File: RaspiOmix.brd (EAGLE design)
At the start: 85 x 56 mm, 48 parts, among them IC1 MCP3424-E/SL, IC2 DS1307

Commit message: Small modif !
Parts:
- moved R27 5.07 mm to (67.5, 20.3), turned to 180 degrees
- moved R26 1.02 mm to (67.5, 18.1)
- moved C5 0.95 mm to (64.1, 19.7)
- moved C30 0.32 mm to (53.3, 35.6)
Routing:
- net PI_SCL: track 87.6 -> 88.6 mm
- net +5V: track 283.7 -> 282.9 mm
- net N$4: track 10.5 -> 9.76 mm

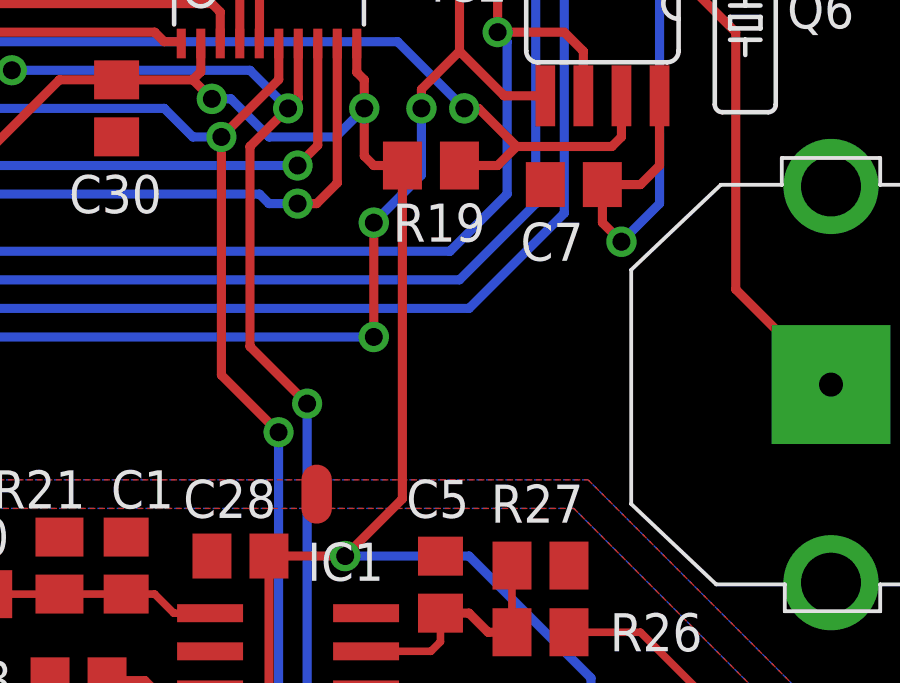
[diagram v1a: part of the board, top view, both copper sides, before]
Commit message: Added C6
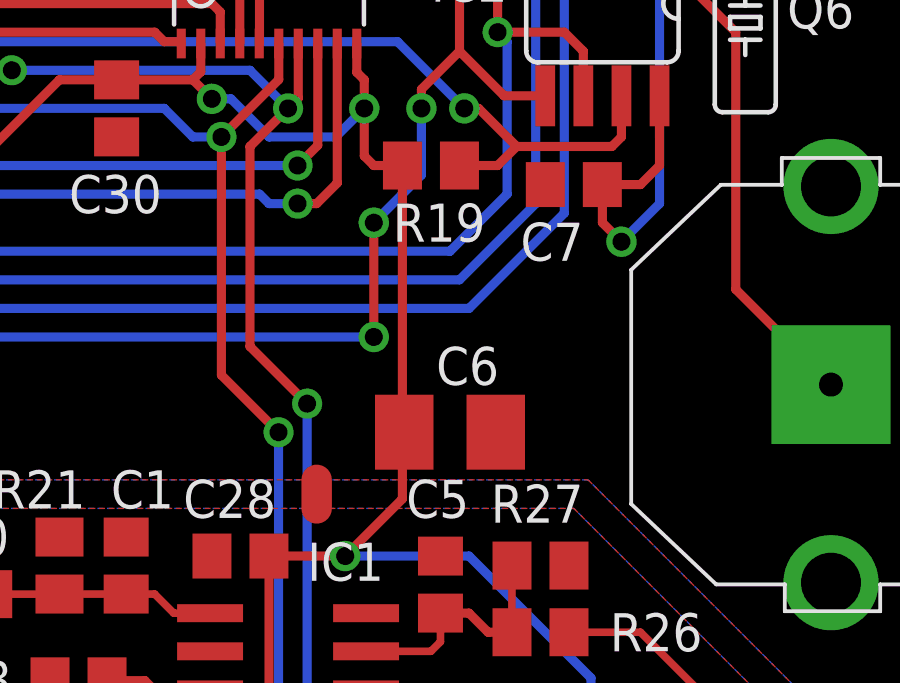
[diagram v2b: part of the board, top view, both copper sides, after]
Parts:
- added C6: (no value), rcl:B/3528-21R
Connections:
- net +3V3: now also C6.+
- net VSS: now also C6.-
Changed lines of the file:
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@@
 <layer number="22" name="bPlace" color="7" fill="1" visible="yes" active="yes"/>
 <layer number="23" name="tOrigins" color="15" fill="1" visible="yes" active="yes"/>
-<layer number="24" name="bOrigins" color="15" fill="1" visible="yes" active="yes"/>
+<layer number="24" name="bOrigins" color="15" fill="1" visible="no" active="yes"/>
 <layer number="25" name="tNames" color="7" fill="1" visible="yes" active="yes"/>
 <layer number="26" name="bNames" color="7" fill="1" visible="yes" active="yes"/>
@@
 <layer number="37" name="tTest" color="7" fill="1" visible="no" active="yes"/>
 <layer number="38" name="bTest" color="7" fill="1" visible="no" active="yes"/>
-<layer number="39" name="tKeepout" color="4" fill="11" visible="yes" active="yes"/>
-<layer number="40" name="bKeepout" color="1" fill="11" visible="no" active="yes"/>
-<layer number="41" name="tRestrict" color="4" fill="10" visible="yes" active="yes"/>
-<layer number="42" name="bRestrict" color="1" fill="10" visible="no" active="yes"/>
+<layer number="39" name="tKeepout" color="4" fill="11" visible="no" active="yes"/>
+<layer number="40" name="bKeepout" color="1" fill="11" visible="yes" active="yes"/>
+<layer number="41" name="tRestrict" color="4" fill="10" visible="no" active="yes"/>
+<layer number="42" name="bRestrict" color="1" fill="10" visible="yes" active="yes"/>
 <layer number="43" name="vRestrict" color="2" fill="10" visible="yes" active="yes"/>
 <layer number="44" name="Drills" color="7" fill="1" visible="no" active="yes"/>
@@
 <attribute name="VALUE" x="67.5274" y="10.795" size="0.02" layer="28" rot="MR180"/>
 </element>
+<element name="C6" library="rcl" package="B/3528-21R" value="" x="64.4525" y="24.765" smashed="yes" rot="R180">
+<attribute name="NAME" x="66.085" y="27.61" size="1.27" layer="25" rot="R180"/>
+<attribute name="VALUE" x="66.4025" y="27.69" size="1.27" layer="27" rot="R180"/>
+</element>
 </elements>
 <signals>
@@
 <contactref element="J_ADR0" pad="1"/>
 <contactref element="J_ADR1" pad="1"/>
+<contactref element="C6" pad="-"/>
 <wire x1="8.89" y1="54.61" x2="9.8425" y2="54.9275" width="0" layer="19" extent="1-1"/>
 <wire x1="3.81" y1="49.8475" x2="3.81" y2="48.895" width="0" layer="19" extent="1-16"/>
@@
 <wire x1="62.8675" y1="33.655" x2="62.8675" y2="33.0225" width="0.3048" layer="1"/>
 <wire x1="62.8675" y1="33.0225" x2="62.865" y2="33.02" width="0.3048" layer="1"/>
-<wire x1="62.865" y1="33.02" x2="62.865" y2="22.5425" width="0.3048" layer="1"/>
+<wire x1="62.865" y1="33.02" x2="62.865" y2="24.765" width="0.3048" layer="1"/>
+<wire x1="62.865" y1="24.765" x2="62.865" y2="22.5425" width="0.3048" layer="1"/>
 <wire x1="2.2225" y1="34.925" x2="2.2225" y2="38.4175" width="0.3048" layer="16"/>
 <wire x1="2.2225" y1="38.4175" x2="3.175" y2="39.37" width="0.3048" layer="16"/>
@@
 <wire x1="65.0875" y1="20.6375" x2="60.96" y2="20.6375" width="0.3048" layer="16"/>
 <via x="60.96" y="20.6375" extent="1-16" drill="0.6" diameter="1.016"/>
+<contactref element="C6" pad="+"/>
+<wire x1="62.9275" y1="24.765" x2="62.865" y2="24.765" width="0.254" layer="1"/>
 </signal>
 <signal name="PI_TX">

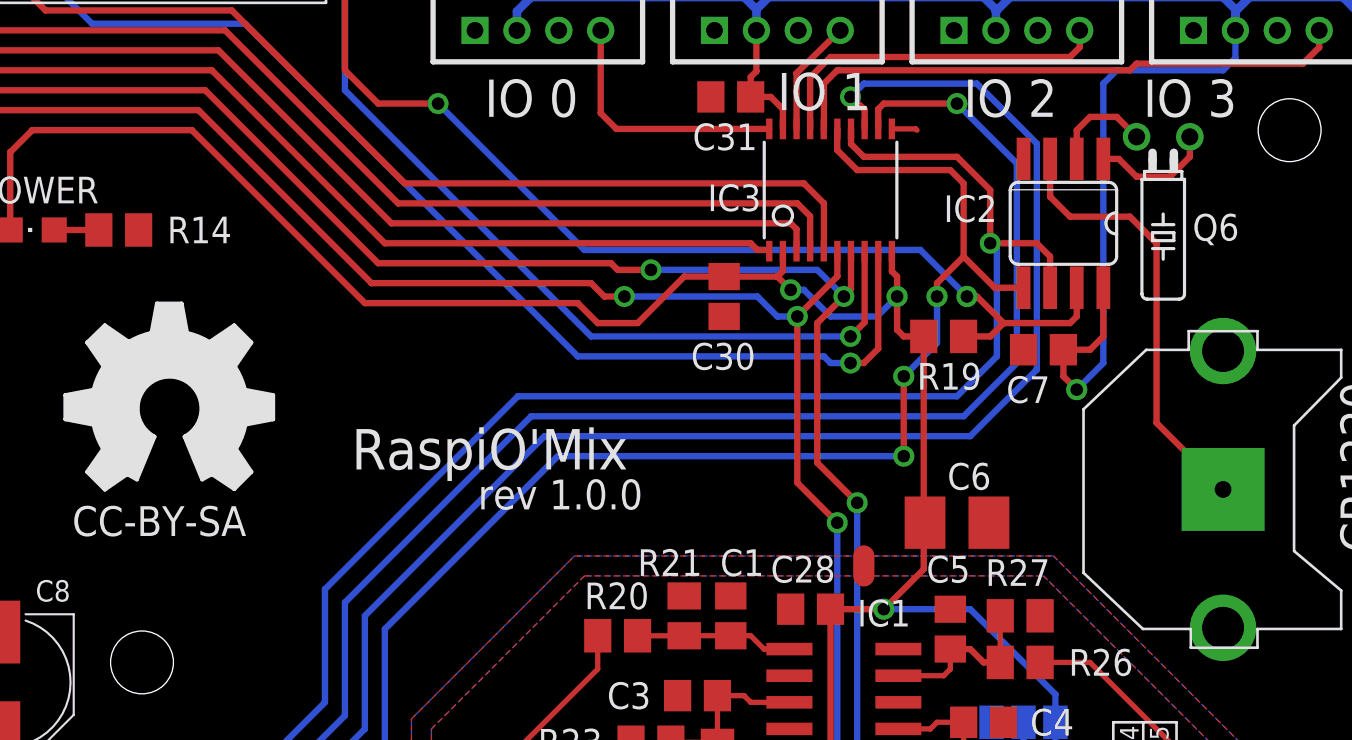
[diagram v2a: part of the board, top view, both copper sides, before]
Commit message: Version avec Mosfet
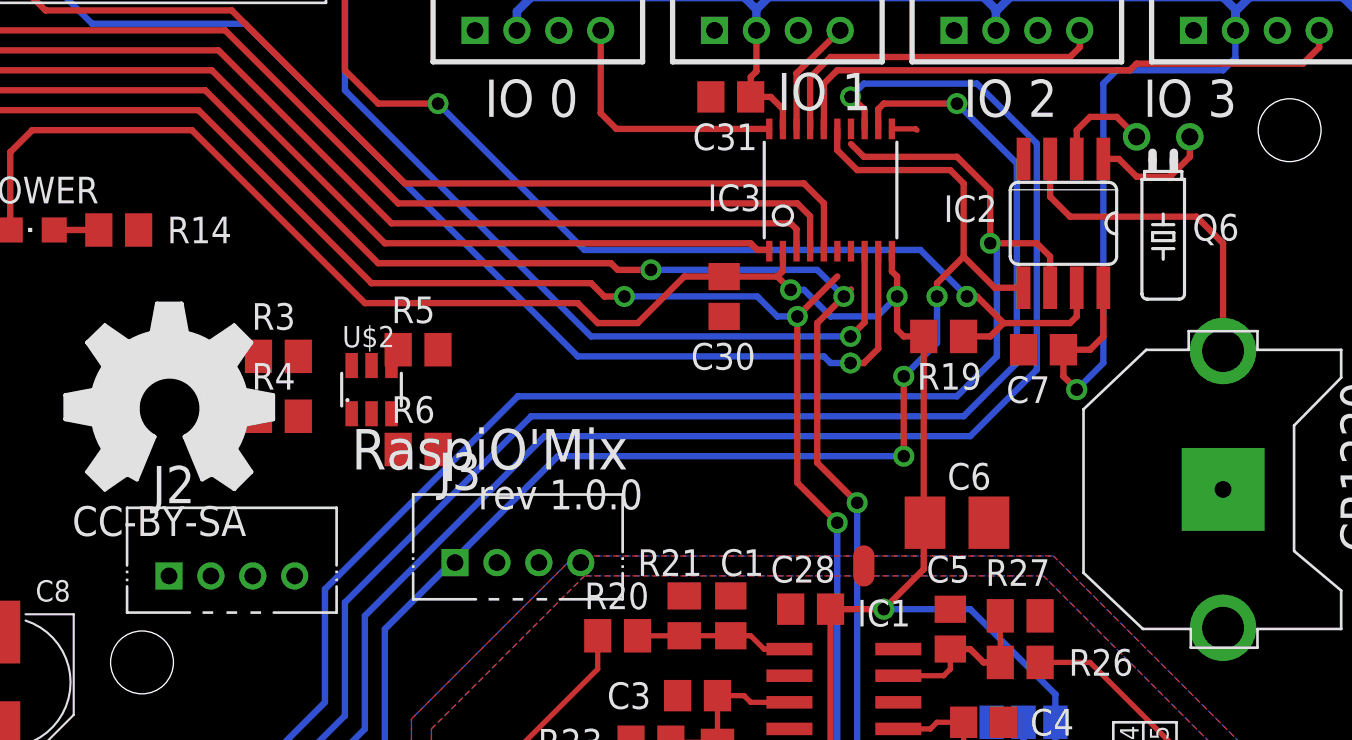
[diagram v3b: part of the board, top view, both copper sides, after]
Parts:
- added J2, J3: (no value), Seeedstudio_Connector:4P-2.0-W/O-BUCKLE
- added R3, R4, R5, R6: 10k, rcl:M0805
- added U$2: FDC6301N, RaspiOMix:SOT23-6
- R19: value 10 -> 1k
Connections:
- removed net PI_CE1: U$3.26
- new net IO4: IC3.15, J2.4
- new net IO5: IC3.14, J3.4
- new net PI_IO4: IC3.6, U$3.22
- new net PI_IO5: IC3.7, U$3.26
- net +3V3: now also R5.2, R6.2, U$2.1, U$2.3
- net +5V: now also J2.2, J3.2, R3.2, R4.2
- net N$58: now also CR1220.+1; no longer CR1220.-
- net PI_SCL: now also R6.1, U$2.2; no longer IC3.7
- net PI_SDA: now also R5.1, U$2.5; no longer IC3.6
- net SCL: now also R4.1, U$2.4; no longer IC3.14
- net SDA: now also R3.1, U$2.6; no longer IC3.15
- net VSS: now also CR1220.-, J2.1, J3.1; no longer CR1220.+1, CR1220.+2
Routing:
- net N$58: track 20.9 -> 16.1 mm
- net PI_SCL: track 88.6 -> 86.7 mm
- net PI_SDA: track 88.7 -> 87.5 mm
- net SCL: track 90.7 -> 90.0 mm
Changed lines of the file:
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@@
 <attribute name="VALUE" x="71.628" y="41.148" size="1.27" layer="27" ratio="10" rot="R270"/>
 </element>
-<element name="R19" library="rcl" package="M0805" value="10" x="63.8175" y="33.655" smashed="yes" rot="R180">
+<element name="R19" library="rcl" package="M0805" value="1k" x="63.8175" y="33.655" smashed="yes" rot="R180">
 <attribute name="NAME" x="62.5475" y="31.115" size="1.27" layer="25"/>
 <attribute name="VALUE" x="65.0875" y="36.195" size="1.27" layer="27" rot="R180"/>
@@
 <attribute name="VALUE" x="66.4025" y="27.69" size="1.27" layer="27" rot="R180"/>
 </element>
+<element name="U$2" library="RaspiOMix" package="SOT23-6" value="FDC6301N" x="36.5125" y="31.115"/>
+<element name="R3" library="rcl" package="M0805" value="10k" x="32.0675" y="32.7025"/>
+<element name="R4" library="rcl" package="M0805" value="10k" x="32.0675" y="29.845"/>
+<element name="R5" library="rcl" package="M0805" value="10k" x="38.735" y="33.02"/>
+<element name="R6" library="rcl" package="M0805" value="10k" x="38.735" y="28.2575"/>
+<element name="J2" library="Seeedstudio_Connector" package="4P-2.0-W/O-BUCKLE" value="" x="29.845" y="22.225"/>
+<element name="J3" library="Seeedstudio_Connector" package="4P-2.0-W/O-BUCKLE" value="" x="43.4975" y="22.86"/>
 </elements>
 <signals>
@@
 <contactref element="R14" pad="1"/>
 <contactref element="IC2" pad="4"/>
-<contactref element="CR1220" pad="+1"/>
-<contactref element="CR1220" pad="+2"/>
 <contactref element="IC3" pad="11"/>
 <contactref element="C30" pad="2"/>
@@
 <contactref element="J_ADR1" pad="1"/>
 <contactref element="C6" pad="-"/>
+<contactref element="CR1220" pad="-"/>
+<contactref element="J3" pad="1"/>
+<contactref element="J2" pad="1"/>
 <wire x1="8.89" y1="54.61" x2="9.8425" y2="54.9275" width="0" layer="19" extent="1-1"/>
 <wire x1="3.81" y1="49.8475" x2="3.81" y2="48.895" width="0" layer="19" extent="1-16"/>
+<wire x1="65.9775" y1="24.765" x2="64.135" y2="20.635" width="0" layer="19" extent="1-1"/>
 </signal>
 <signal name="+5V">
@@
 <wire x1="12.3825" y1="24.4475" x2="13.795" y2="23.035" width="0.4064" layer="1"/>
 <wire x1="13.795" y1="19.685" x2="13.795" y2="23.035" width="0.4064" layer="1"/>
-<wire x1="3.81" y1="45.72" x2="3.81" y2="44.2725" width="0" layer="19" extent="1-1"/>
-<wire x1="19.05" y1="14.745" x2="18.3575" y2="14.9225" width="0" layer="19" extent="1-1"/>
+<contactref element="R3" pad="2"/>
+<contactref element="R4" pad="2"/>
+<contactref element="J2" pad="2"/>
+<contactref element="J3" pad="2"/>
+<wire x1="33.0175" y1="29.845" x2="42.4975" y2="22.86" width="0" layer="19" extent="1-1"/>
+<wire x1="33.0175" y1="32.7025" x2="33.0175" y2="29.845" width="0" layer="19" extent="1-1"/>
+<wire x1="28.845" y1="22.225" x2="33.0175" y2="29.845" width="0" layer="19" extent="1-1"/>
+<wire x1="19.05" y1="14.745" x2="28.845" y2="22.225" width="0" layer="19" extent="1-1"/>
+<wire x1="18.3575" y1="14.9225" x2="19.05" y2="14.745" width="0" layer="19" extent="1-1"/>
+<wire x1="3.81" y1="44.2725" x2="3.81" y2="45.72" width="0" layer="19" extent="1-1"/>
 </signal>
 <signal name="SDA">
@@
 <contactref element="CON_I2C_0" pad="3"/>
 <contactref element="CON_I2C_1" pad="3"/>
-<contactref element="IC3" pad="15"/>
 <wire x1="64.77" y1="37.465" x2="64.77" y2="40.9575" width="0.3048" layer="1"/>
 <wire x1="64.77" y1="40.9575" x2="64.135" y2="41.5925" width="0.3048" layer="1"/>
@@
 <wire x1="59.69" y1="41.5925" x2="58.7375" y2="42.545" width="0.3048" layer="1"/>
 <wire x1="58.7375" y1="42.545" x2="58.7375" y2="43.5503" width="0.3048" layer="1"/>
-<wire x1="58.7375" y1="43.5503" x2="58.745" y2="43.5578" width="0.3048" layer="1"/>
 <wire x1="29.5275" y1="10.4775" x2="33.3375" y2="10.4775" width="0.3048" layer="16"/>
 <wire x1="33.3375" y1="10.4775" x2="37.1475" y2="14.2875" width="0.3048" layer="16"/>
@@
 <wire x1="61.9125" y1="31.75" x2="61.9125" y2="27.94" width="0.3048" layer="1"/>
 <via x="61.9125" y="27.94" extent="1-16" drill="0.6" diameter="1.016"/>
+<contactref element="U$2" pad="6"/>
+<contactref element="R3" pad="1"/>
+<wire x1="31.1175" y1="32.7025" x2="35.5625" y2="32.265" width="0" layer="19" extent="1-1"/>
+<wire x1="45.4025" y1="27.94" x2="35.5625" y2="32.265" width="0" layer="19" extent="1-16"/>
 </signal>
 <signal name="SCL">
 <contactref element="IC2" pad="6"/>
-<contactref element="IC3" pad="14"/>
-<wire x1="59.395" y1="43.5578" x2="59.395" y2="42.84" width="0.3048" layer="1"/>
 <wire x1="59.395" y1="42.84" x2="60.0075" y2="42.2275" width="0.3048" layer="1"/>
 <wire x1="60.0075" y1="42.2275" x2="64.4525" y2="42.2275" width="0.3048" layer="1"/>
@@
 <wire x1="64.4525" y1="30.7975" x2="66.3575" y2="32.7025" width="0.3048" layer="16"/>
 <wire x1="14.78" y1="7.1275" x2="14.78" y2="7.9375" width="0.3048" layer="1"/>
+<contactref element="U$2" pad="4"/>
+<contactref element="R4" pad="1"/>
+<wire x1="43.4975" y1="30.7975" x2="37.4625" y2="32.265" width="0" layer="19" extent="1-16"/>
+<wire x1="31.1175" y1="29.845" x2="37.4625" y2="32.265" width="0" layer="19" extent="1-1"/>
 </signal>
 <signal name="+3V3">
@@
 <contactref element="C6" pad="+"/>
 <wire x1="62.9275" y1="24.765" x2="62.865" y2="24.765" width="0.254" layer="1"/>
+<contactref element="R5" pad="2"/>
+<contactref element="U$2" pad="1"/>
+<contactref element="R6" pad="2"/>
+<contactref element="U$2" pad="3"/>
+<wire x1="37.4625" y1="29.965" x2="39.685" y2="33.02" width="0" layer="19" extent="1-1"/>
+<wire x1="35.5625" y1="29.965" x2="37.4625" y2="29.965" width="0" layer="19" extent="1-1"/>
+<wire x1="39.685" y1="28.2575" x2="37.4625" y2="29.965" width="0" layer="19" extent="1-1"/>
+<wire x1="36.195" y1="35.2425" x2="39.685" y2="33.02" width="0" layer="19" extent="1-1"/>
 </signal>
 <signal name="PI_TX">
@@
 <contactref element="U$3" pad="3"/>
 <contactref element="IC1" pad="7"/>
-<contactref element="IC3" pad="6"/>
 <wire x1="5.08" y1="50.8" x2="6.6675" y2="49.2125" width="0.3048" layer="1"/>
 <wire x1="6.6675" y1="49.2125" x2="7.62" y2="49.2125" width="0.3048" layer="1"/>
@@
 <wire x1="58.7375" y1="24.765" x2="56.8325" y2="26.67" width="0.3048" layer="1"/>
 <wire x1="56.8325" y1="26.67" x2="56.8325" y2="34.6075" width="0.3048" layer="1"/>
-<wire x1="58.745" y1="37.7222" x2="58.745" y2="36.52" width="0.3048" layer="1"/>
 <wire x1="58.745" y1="36.52" x2="56.8325" y2="34.6075" width="0.3048" layer="1"/>
 <wire x1="56.455" y1="11.1125" x2="58.42" y2="11.1125" width="0.3048" layer="1"/>
@@
 <wire x1="55.88" y1="34.6075" x2="56.8325" y2="34.6075" width="0.3048" layer="16"/>
 <via x="56.8325" y="34.6075" extent="1-16" drill="0.6"/>
+<contactref element="U$2" pad="5"/>
+<contactref element="R5" pad="1"/>
+<wire x1="36.5125" y1="32.265" x2="37.785" y2="33.02" width="0" layer="19" extent="1-1"/>
+<wire x1="36.5125" y1="36.195" x2="37.785" y2="33.02" width="0" layer="19" extent="1-1"/>
 </signal>
 <signal name="PI_SCL">
 <contactref element="U$3" pad="5"/>
 <contactref element="IC1" pad="8"/>
-<contactref element="IC3" pad="7"/>
 <wire x1="7.62" y1="50.8" x2="10.16" y2="48.26" width="0.3048" layer="1"/>
 <wire x1="10.16" y1="48.26" x2="13.6525" y2="48.26" width="0.3048" layer="1"/>
@@
 <wire x1="47.9425" y1="37.1475" x2="48.26" y2="36.83" width="0.3048" layer="1"/>
 <wire x1="48.26" y1="36.83" x2="49.8475" y2="36.83" width="0.3048" layer="1"/>
-<wire x1="59.395" y1="37.7222" x2="59.395" y2="35.9" width="0.3048" layer="1"/>
 <wire x1="57.785" y1="34.29" x2="57.785" y2="27.6225" width="0.3048" layer="1"/>
 <wire x1="57.785" y1="27.6225" x2="59.69" y2="25.7175" width="0.3048" layer="1"/>
@@
 <wire x1="59.395" y1="35.9" x2="59.055" y2="35.56" width="0.3048" layer="1"/>
 <wire x1="59.055" y1="35.56" x2="57.785" y2="34.29" width="0.3048" layer="1"/>
+<contactref element="U$2" pad="2"/>
+<contactref element="R6" pad="1"/>
+<wire x1="37.785" y1="28.2575" x2="36.5125" y2="29.965" width="0" layer="19" extent="1-1"/>
+<wire x1="36.83" y1="37.1475" x2="36.5125" y2="29.965" width="0" layer="19" extent="1-1"/>
 </signal>
 <signal name="N$33">
@@
 <signal name="N$58">
 <contactref element="IC2" pad="3"/>
-<contactref element="CR1220" pad="-"/>
 <wire x1="68.8975" y1="42.1259" x2="68.8975" y2="40.3225" width="0.3048" layer="1"/>
 <wire x1="68.8975" y1="40.3225" x2="69.85" y2="39.37" width="0.3048" layer="1"/>
-<wire x1="69.85" y1="39.37" x2="72.7075" y2="39.37" width="0.3048" layer="1"/>
-<wire x1="72.7075" y1="39.37" x2="73.9775" y2="38.1" width="0.3048" layer="1"/>
-<wire x1="73.9775" y1="38.1" x2="73.9775" y2="29.5275" width="0.3048" layer="1"/>
-<wire x1="73.9775" y1="29.5275" x2="77.1525" y2="26.3525" width="0.3048" layer="1"/>
+<contactref element="CR1220" pad="+1"/>
+<wire x1="77.1525" y1="32.9565" x2="77.1525" y2="38.1" width="0.3048" layer="1"/>
+<wire x1="77.1525" y1="38.1" x2="75.8825" y2="39.37" width="0.3048" layer="1"/>
+<wire x1="75.8825" y1="39.37" x2="69.85" y2="39.37" width="0.3048" layer="1"/>
 </signal>
 <signal name="INTC">
@@
 <contactref element="U$3" pad="23"/>
 </signal>
-<signal name="PI_CE1">
+<signal name="PI_IO5">
 <contactref element="U$3" pad="26"/>
+<contactref element="IC3" pad="7"/>
+<wire x1="33.02" y1="53.34" x2="59.395" y2="37.7222" width="0" layer="19" extent="1-1"/>
 </signal>
 <signal name="PI_CE0">
@@
 <via x="63.5" y="13.6525" extent="1-16" drill="0.6" diameter="1.016"/>
 </signal>
+<signal name="PI_IO4">
+<contactref element="U$3" pad="22"/>
+<contactref element="IC3" pad="6"/>
+<wire x1="27.94" y1="53.34" x2="58.745" y2="37.7222" width="0" layer="19" extent="1-1"/>
+</signal>
+<signal name="IO4">
+<contactref element="IC3" pad="15"/>
+<contactref element="J2" pad="4"/>
+<wire x1="32.845" y1="22.225" x2="58.745" y2="43.5578" width="0" layer="19" extent="1-1"/>
+</signal>
+<signal name="IO5">
+<contactref element="IC3" pad="14"/>
+<contactref element="J3" pad="4"/>
+<wire x1="46.4975" y1="22.86" x2="59.395" y2="43.5578" width="0" layer="19" extent="1-1"/>
+</signal>
 </signals>

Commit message: Version 1.0.0
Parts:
- removed J2, J3: (no value), Seeedstudio_Connector:4P-2.0-W/O-BUCKLE
- removed R3, R4, R5, R6: 10k, rcl:M0805
- removed U$2: FDC6301N, RaspiOMix:SOT23-6
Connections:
- removed net IO4: IC3.15, J2.4
- removed net IO5: IC3.14, J3.4
- removed net PI_IO4: IC3.6, U$3.22
- removed net PI_IO5: IC3.7, U$3.26
- new net PI_CE1: U$3.26
- net +3V3: no longer R5.2, R6.2, U$2.1, U$2.3
- net +5V: no longer J2.2, J3.2, R3.2, R4.2
- net PI_SCL: now also IC3.7; no longer R6.1, U$2.2
- net PI_SDA: now also IC3.6; no longer R5.1, U$2.5
- net SCL: now also IC3.14; no longer R4.1, U$2.4
- net SDA: now also IC3.15; no longer R3.1, U$2.6
- net VSS: no longer J2.1, J3.1
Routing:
- net PI_SCL: track 86.7 -> 88.6 mm
- net PI_SDA: track 87.5 -> 88.7 mm
- net SCL: track 90.0 -> 90.7 mm
